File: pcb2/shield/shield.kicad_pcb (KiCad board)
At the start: 2 copper layers, 50 x 50 mm, 29 parts, among them IC1 STM32F0xxKxTx, IC2 MCP1700, IC3 AM26C31, IC4 AM26C31, J1 MICROUSB, P1 SWD_TC, P10 BUS5, P11 BUS6, P12 BUS7, P13 BUS8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

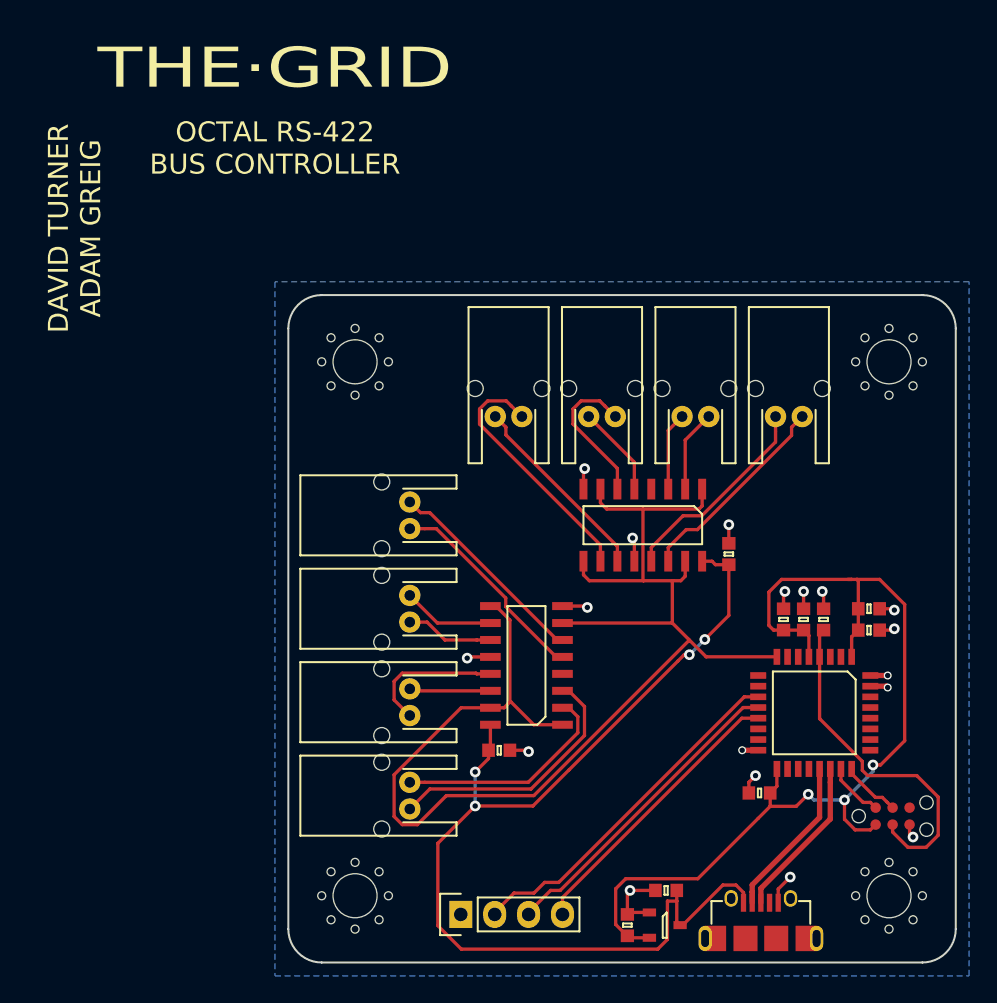
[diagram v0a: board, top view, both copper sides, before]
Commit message: Ground planes and stitching
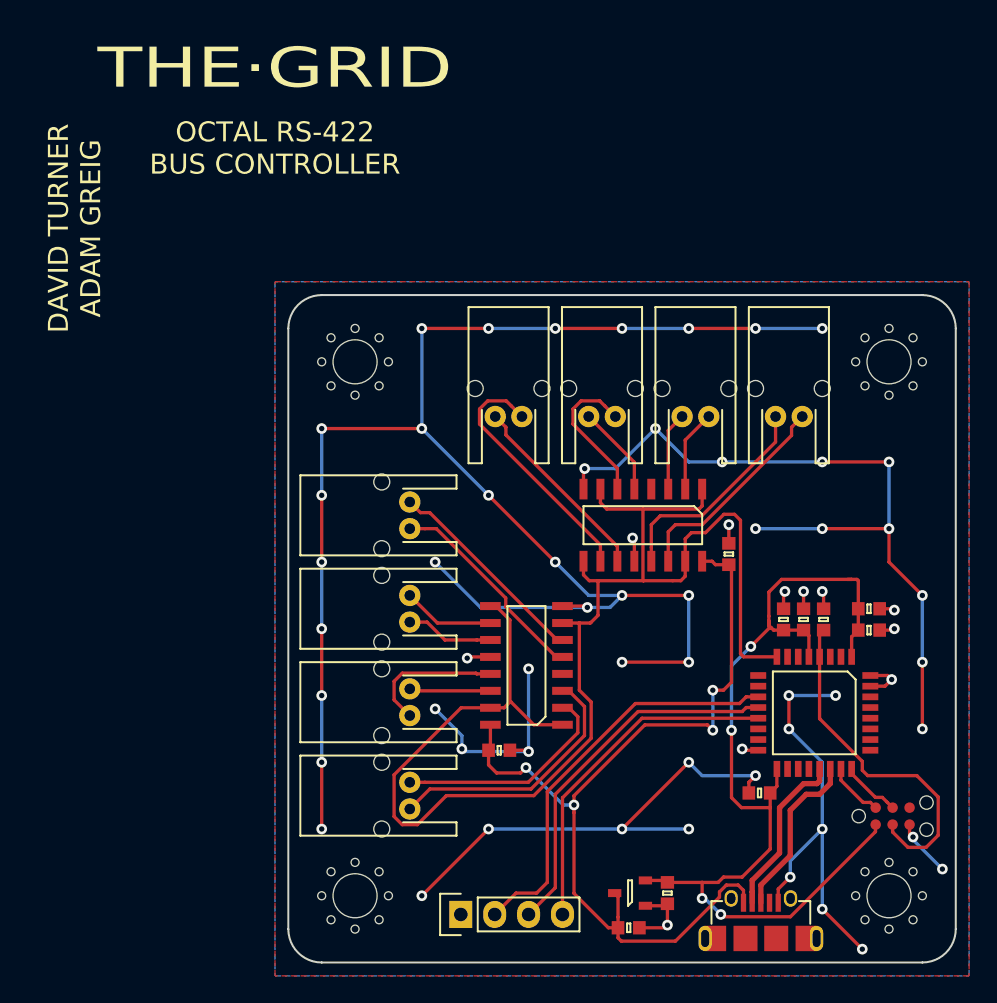
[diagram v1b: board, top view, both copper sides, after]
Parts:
- moved C9 3.96 mm to (85.5, 107.4), turned to 0 degrees
- moved C10 3.84 mm to (88.4, 104.8), turned to 270 degrees
- moved IC2 3.54 mm to (85.6, 104.8), turned to 180 degrees
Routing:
- net GND: track 30.3 -> 295.7 mm, vias 18 -> 64
- net +5V: track 79.1 -> 67.5 mm
- net /SHIFT_DATA: track 21.5 -> 25.9 mm
- net /SHIFT_SRCK: track 23.7 -> 27.9 mm
- net /SHIFT_RCK: track 26.6 -> 30.6 mm
- net /TX: track 102.7 -> 106.7 mm
- net +3V3: track 75.1 -> 73.0 mm, vias 3 -> 4
- net Net-(IC4-Pad13): track 15.5 -> 16.5 mm
- net Net-(IC4-Pad14): track 15.5 -> 16.2 mm
- net /USB_D-: track 12.1 -> 12.7 mm
- net /USB_D+: track 12.2 -> 12.8 mm
- added copper zone on F.Cu, net GND

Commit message: Shield PCB r2 nominally finished.
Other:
- net class Default: clearance 0.25 -> 0.2
- rule trace_clearance: 0.25 -> 0.2
- board text added: "2016-07-24"
- board text added: "8-WAY RS-422 BUS CONTROLLER"
- board text added: "Revision 2"
- board text removed: "-DATA"
- board text removed: "-RCK"
- board text removed: "-SRCK"
- board text removed: "2016-03-28"
- board text removed: "OCTAL RS-422 BUS CONTROLLER"
- board text removed: "Revision 1"
- board text removed: "THE·GRID"
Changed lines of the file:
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@@
     (links 69)
     (no_connects 0)
-    (area 41.57 34.845 111.000001 113.0925)
+    (area 59.924999 59.924999 110.075001 110.075001)
     (thickness 1.6)
-    (drawings 17)
+    (drawings 13)
     (tracks 436)
     (zones 0)
@@
     (user_trace_width 0.4)
     (user_trace_width 0.5)
-    (trace_clearance 0.25)
+    (trace_clearance 0.2)
     (zone_clearance 0.35)
     (zone_45_only no)
@@
   (net 50 "Net-(P1-Pad6)")
   (net_class Default "This is the default net class."
-    (clearance 0.25)
+    (clearance 0.2)
     (trace_width 0.25)
     (via_dia 0.8)
@@
   (module agg:0603 (layer F.Cu)
     (at 88.4 104.8 270)
-    (fp_text reference C10 (at -2.225 0 360) (layer F.Fab)
-      (effects (font (size 1 1) (thickness 0.15)))
-    )
-    (fp_text value 1u (at 2.225 0 360) (layer F.Fab)
+    (fp_text reference C10 (at -2.225 0) (layer F.Fab)
+      (effects (font (size 1 1) (thickness 0.15)))
+    )
+    (fp_text value 1u (at 2.225 0) (layer F.Fab)
       (effects (font (size 1 1) (thickness 0.15)))
     )
@@
   (gr_line (start 107.5 110) (end 62.5 110) (layer Edge.Cuts) (width 0.15))
   (gr_arc (start 107.5 107.5) (end 110 107.5) (angle 90) (layer Edge.Cuts) (width 0.15))
-  (gr_text -DATA (at 91.5 37 90) (layer B.SilkS)
-    (effects (font (size 1.5 1.5) (thickness 0.3)) (justify left mirror))
-  )
-  (gr_text -SRCK (at 89 37 90) (layer B.SilkS)
-    (effects (font (size 1.5 1.5) (thickness 0.3)) (justify left mirror))
-  )
-  (gr_text -RCK (at 86.5 37 90) (layer B.SilkS)
-    (effects (font (size 1.5 1.5) (thickness 0.3)) (justify left mirror))
-  )
-  (gr_text "1 GND\n2 RCK\n3 SRCK\n4 DATA" (at 83 42) (layer B.SilkS)
+  (gr_text "1 GND\n2 RCK\n3 SRCK\n4 DATA" (at 76.8 96.6 90) (layer B.SilkS)
     (effects (font (size 1.7 1.5) (thickness 0.3)) (justify left mirror))
   )
-  (gr_text "Revision 1" (at 103 36) (layer B.SilkS)
+  (gr_text "Revision 2" (at 82.4 85.6) (layer B.SilkS)
     (effects (font (size 1.5 1.5) (thickness 0.3)) (justify mirror))
   )
-  (gr_text 2016-03-28 (at 103 40) (layer B.SilkS)
+  (gr_text 2016-07-24 (at 81.8 91.2) (layer B.SilkS)
     (effects (font (size 1.5 1.5) (thickness 0.3)) (justify mirror))
   )
-  (gr_text "DAVID TURNER\nADAM GREIG" (at 44 55 90) (layer F.SilkS)
+  (gr_text "DAVID TURNER\nADAM GREIG" (at 101.6 77.4) (layer F.SilkS)
     (effects (font (size 1.5 1.5) (thickness 0.3)))
   )
-  (gr_text "OCTAL RS-422\nBUS CONTROLLER" (at 59 49) (layer F.SilkS)
+  (gr_text "8-WAY RS-422\nBUS CONTROLLER" (at 82.2 100) (layer F.SilkS)
     (effects (font (size 1.5 1.5) (thickness 0.3)))
   )
-  (gr_text THE·GRID (at 59 43) (layer F.SilkS)
-    (effects (font (size 3 4) (thickness 0.5)))
-  )
   (segment (start 89.731227 79.93785) (end 89.731227 78.268773) (width 0.25) (layer F.Cu) (net 1))
